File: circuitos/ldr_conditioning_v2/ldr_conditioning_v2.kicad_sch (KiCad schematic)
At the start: 12 parts, among them J1 Screw_Terminal_01x02, J2 Conn_01x03_Pin, U1 LM358, U2 4066

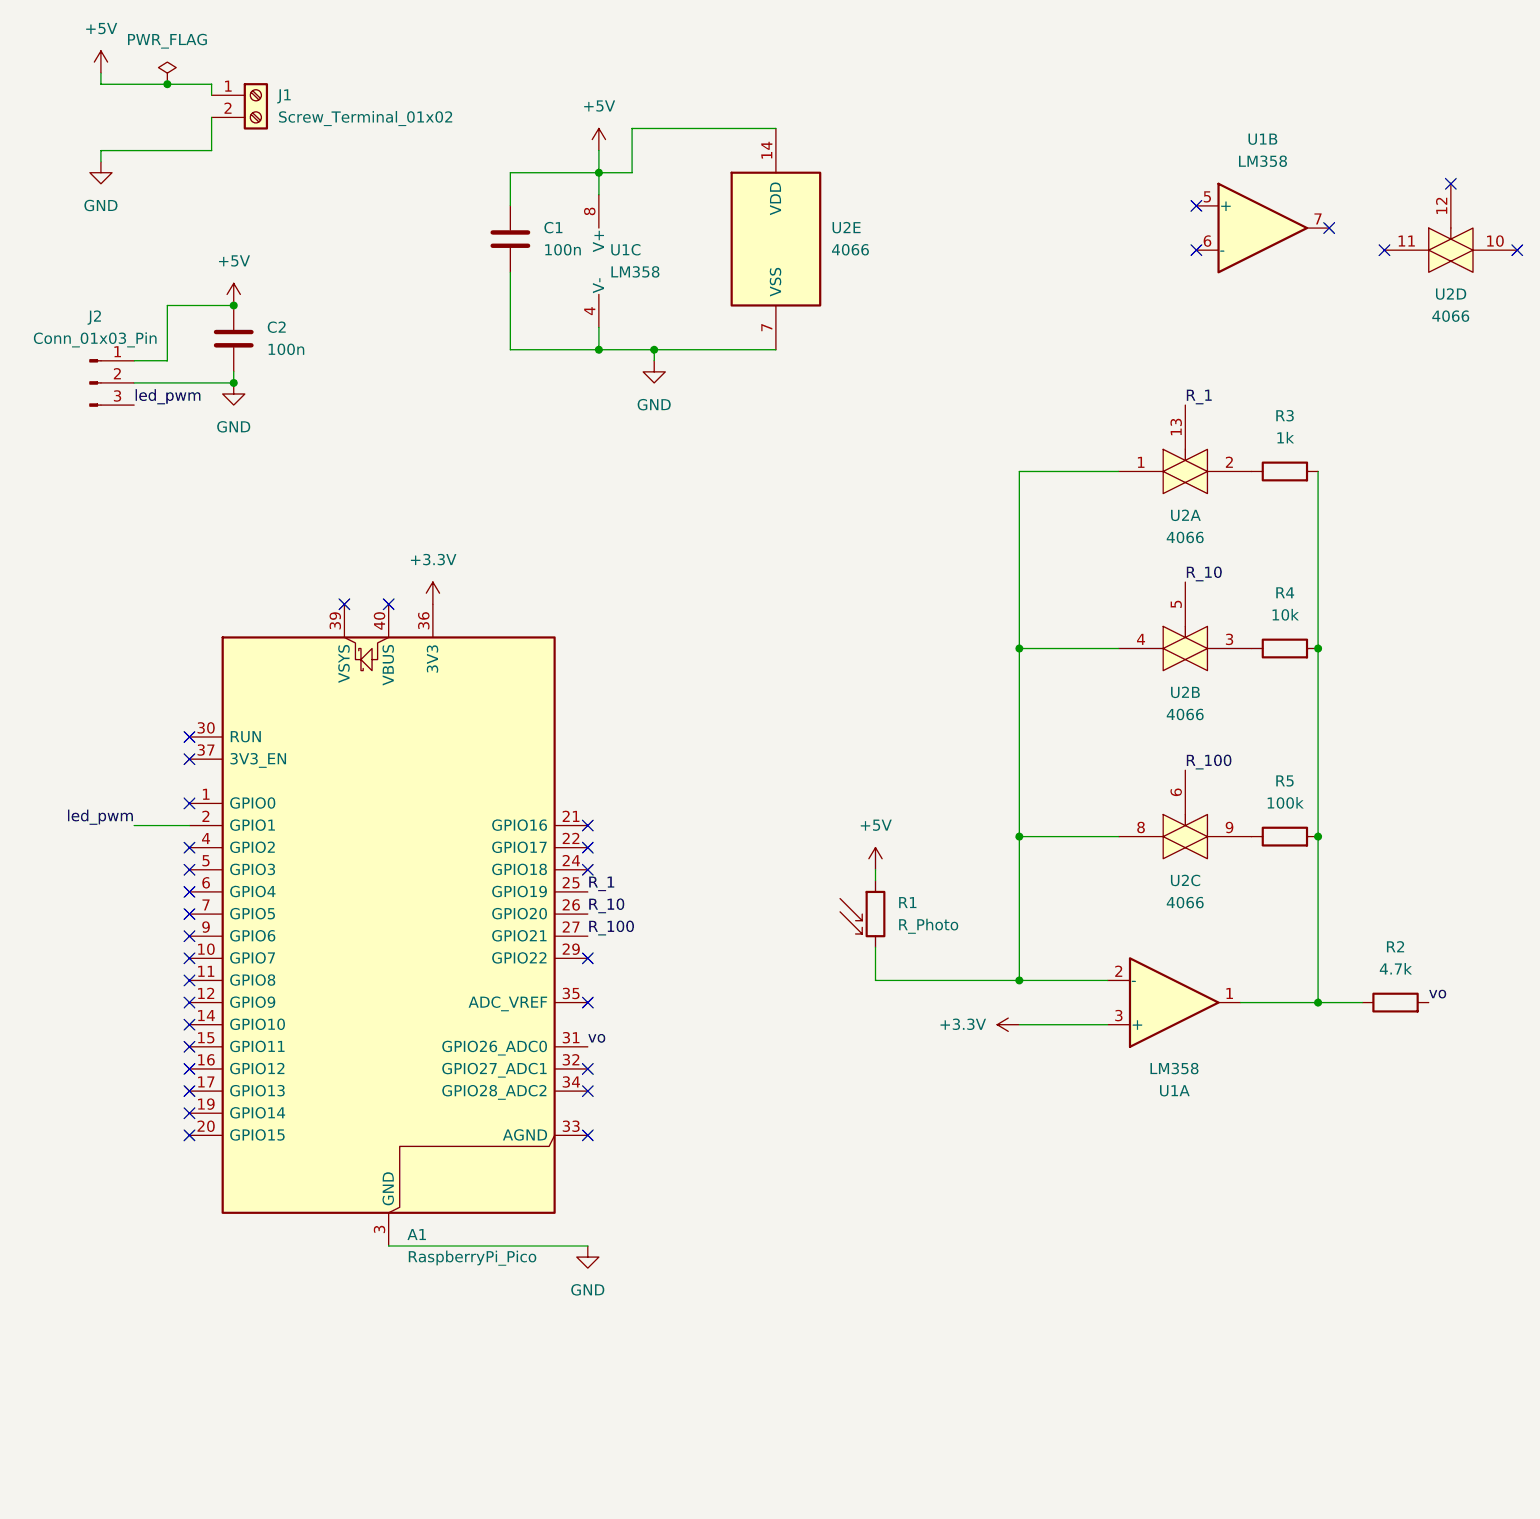
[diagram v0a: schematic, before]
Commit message: esquematico actualizado + pico usb-c sym
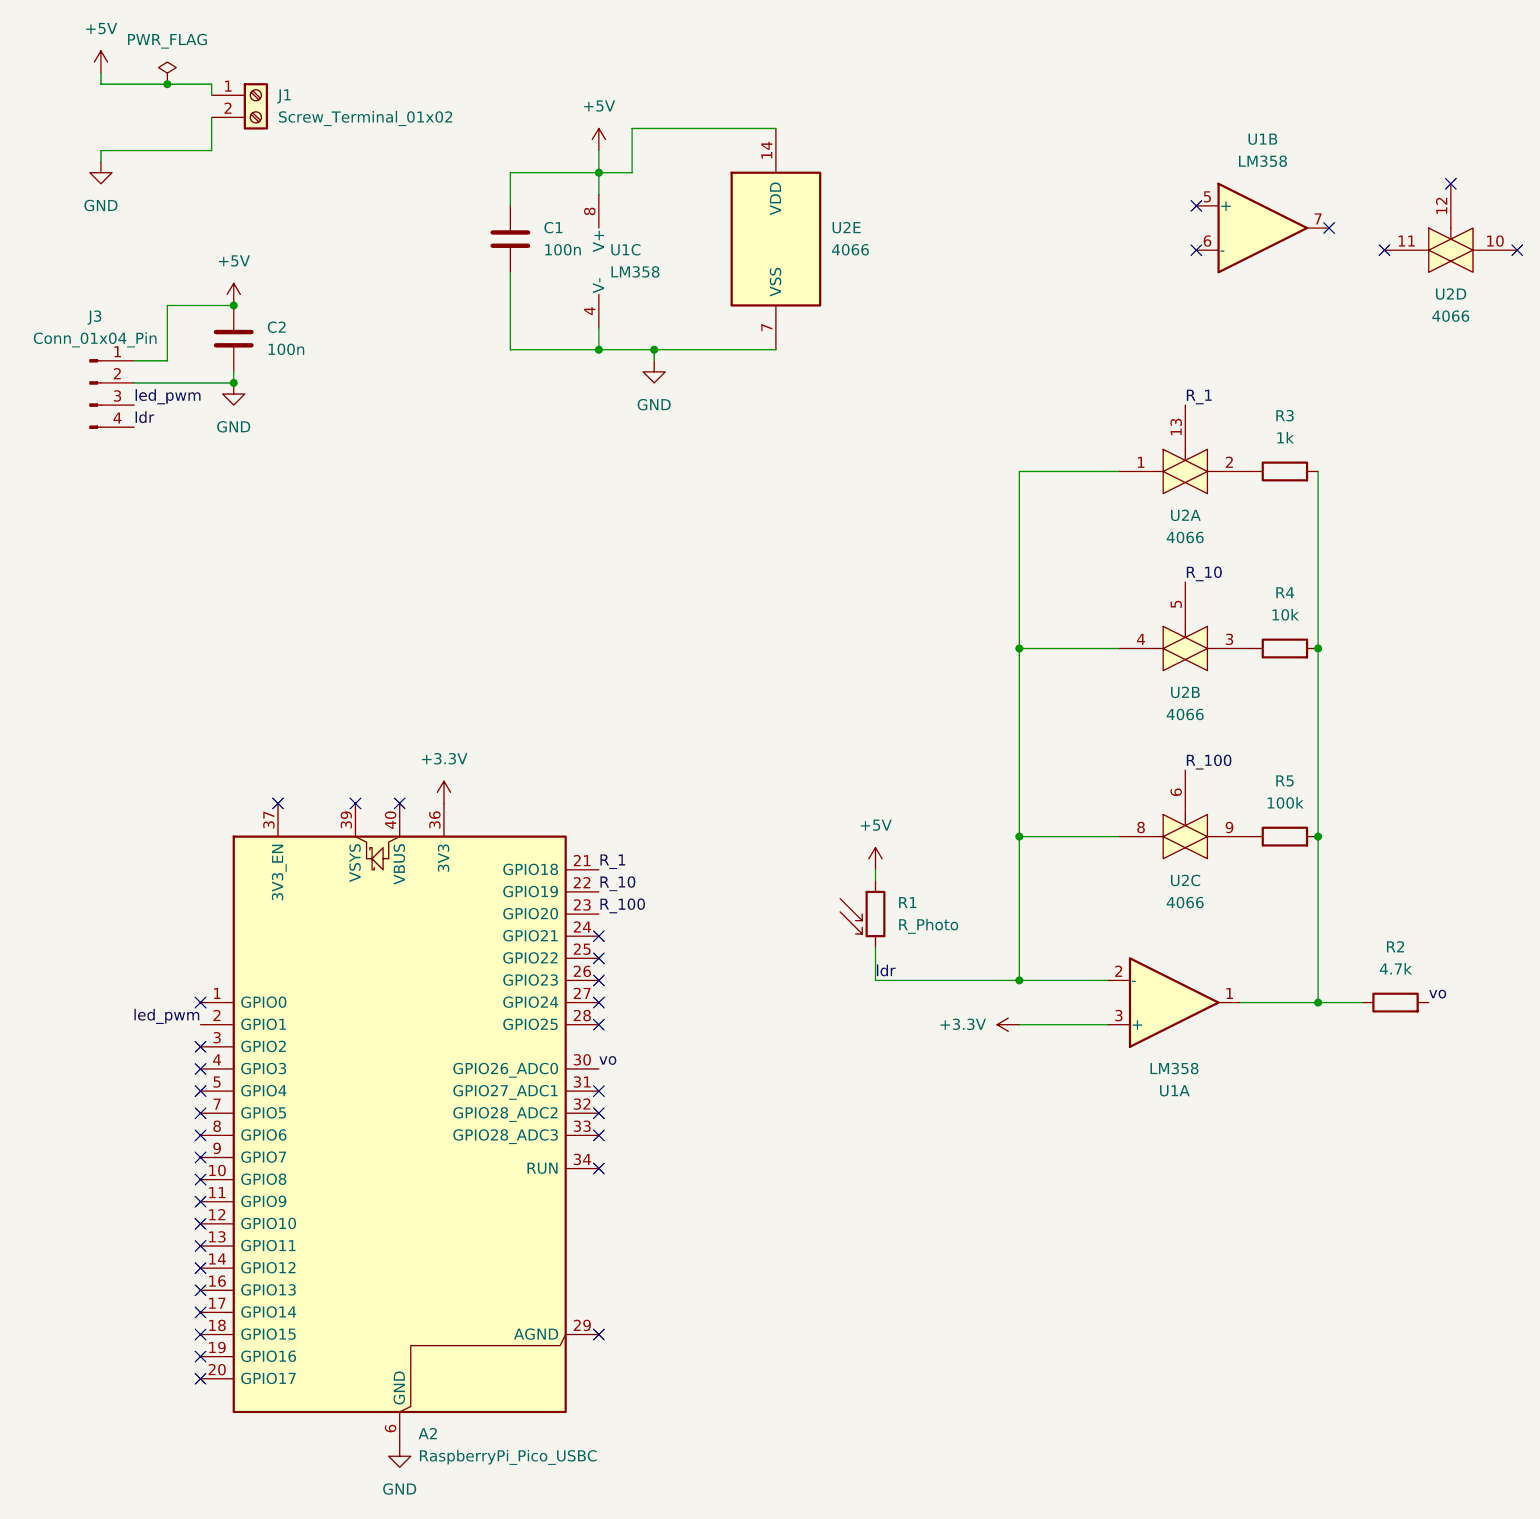
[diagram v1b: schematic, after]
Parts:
- removed A1: RaspberryPi_Pico, Module:RaspberryPi_Pico_Common_Unspecified, symbol MCU_Module:RaspberryPi_Pico
- removed J2: Conn_01x03_Pin, symbol Connector:Conn_01x03_Pin
- added A2: RaspberryPi_Pico_USBC, Module:RaspberryPi_Pico_Common_Unspecified, symbol custom_symbols:RaspberryPi_Pico_USBC
- added J3: Conn_01x04_Pin, Connector_PinHeader_2.54mm:PinHeader_1x04_P2.54mm_Vertical, symbol Connector:Conn_01x04_Pin
- C1, C2: footprint (none) -> Capacitor_THT:C_Disc_D5.0mm_W2.5mm_P2.50mm
- J1: footprint (none) -> TerminalBlock:TerminalBlock_Altech_AK300-2_P5.00mm
- R1, R2, R3, R4, R5: footprint (none) -> Resistor_THT:R_Axial_DIN0207_L6.3mm_D2.5mm_P10.16mm_Horizontal
- U1: footprint (none) -> Package_DIP:DIP-8_W7.62mm_Socket
- U2: footprint (none) -> Package_DIP:DIP-14_W7.62mm_Socket
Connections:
- net +3.3V: now also A2.36 (3V3)
- net +5V: now also J3.1 (Pin_1)
- net GND: now also A2.15 (GND), A2.35 (GND), A2.38 (GND), A2.6 (GND), J3.2 (Pin_2)
- net R_1: now also A2.21 (GPIO18)
- net R_10: now also A2.22 (GPIO19)
- net R_100: now also A2.23 (GPIO20)
- net led_pwm: now also A2.2 (GPIO1), J3.3 (Pin_3)
- net vo: now also A2.30 (GPIO26_ADC0)
- net ldr: now reaches R1.2, U1.2 (-), U2.1, U2.4, U2.8
- net ldr: now also J3.4 (Pin_4)
- no-connect marks 33 -> 36
